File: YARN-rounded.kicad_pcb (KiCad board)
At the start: 2 copper layers, 99 x 91.7 mm, 12 parts, among them J1 Cart System Out, J2 Cart Main In, J3 Cart Sub In, SW1 SW_SPDT, U1 74HC244, U2 74HC244

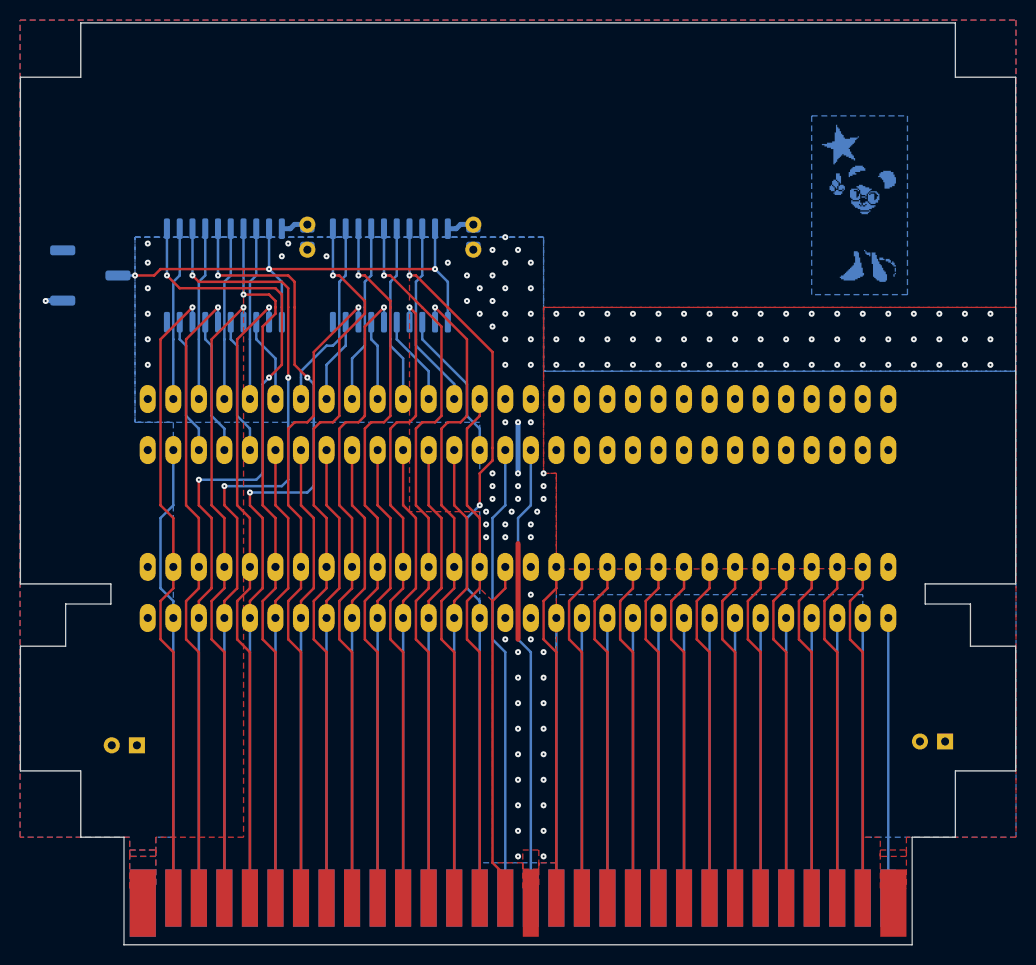
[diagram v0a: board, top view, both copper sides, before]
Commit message: Use bus buffers instead of decoding logic
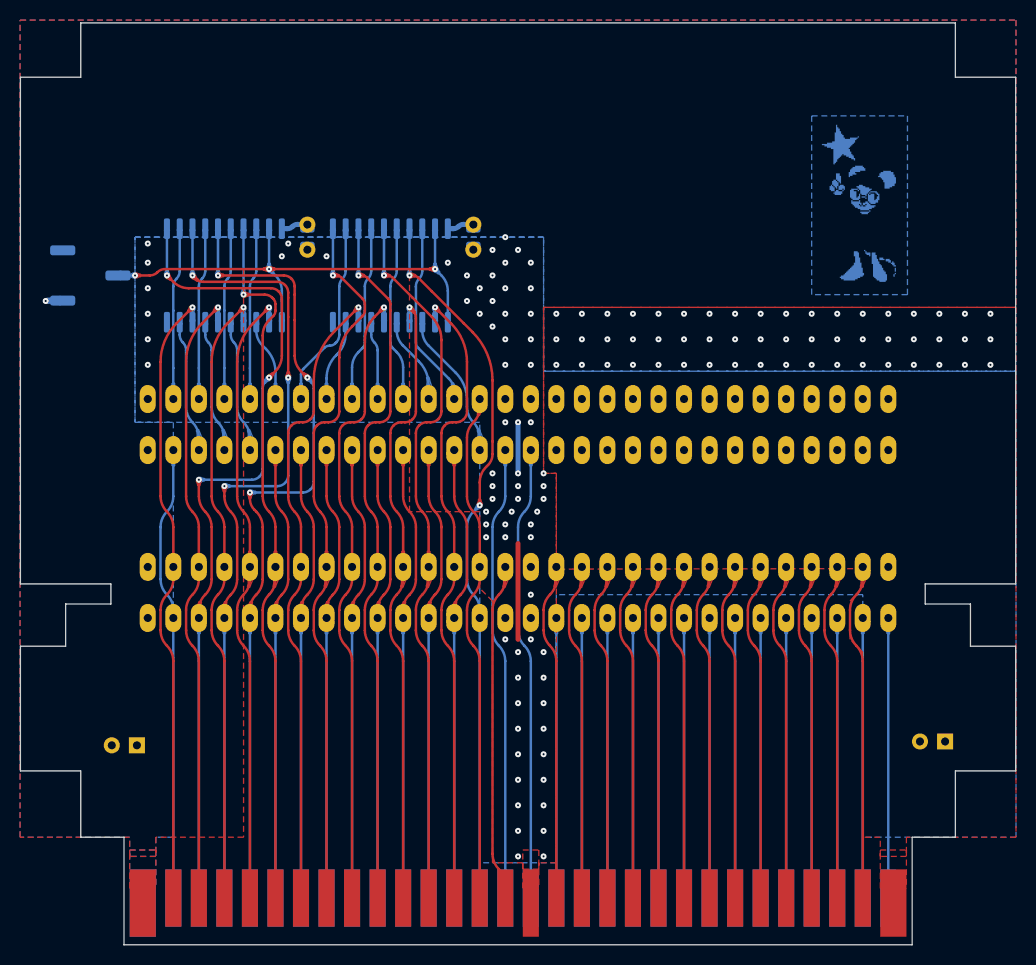
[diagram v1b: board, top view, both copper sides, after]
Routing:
- net /CPU_A6: track 65.4 -> 64.3 mm
- net /CPU_A5: track 72.7 -> 71.5 mm
- net /CPU_A0: track 64.9 -> 63.8 mm
- net /CPU_A1: track 72.7 -> 71.7 mm
- net /CPU_A4: track 64.4 -> 63.4 mm
- net /CPU_A3: track 71.6 -> 70.7 mm
- net /CPU_A2: track 63.9 -> 63.0 mm
- net /CPU_A9: track 63.1 -> 62.2 mm
- net /CPU_A11: track 63.1 -> 62.2 mm
- net /CPU_A10: track 63.1 -> 62.2 mm
- net /CPU_A8: track 63.1 -> 62.2 mm
- net /CPU_A12: track 84.7 -> 83.8 mm
- net /CPU_A7: track 71.5 -> 70.6 mm
- net /~{ROMSEL}: track 71.9 -> 71.1 mm
- net /CPU_R~{W}: track 51.7 -> 50.9 mm
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
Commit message: Buffer data and addr bus, add switch for VRC6 A/B
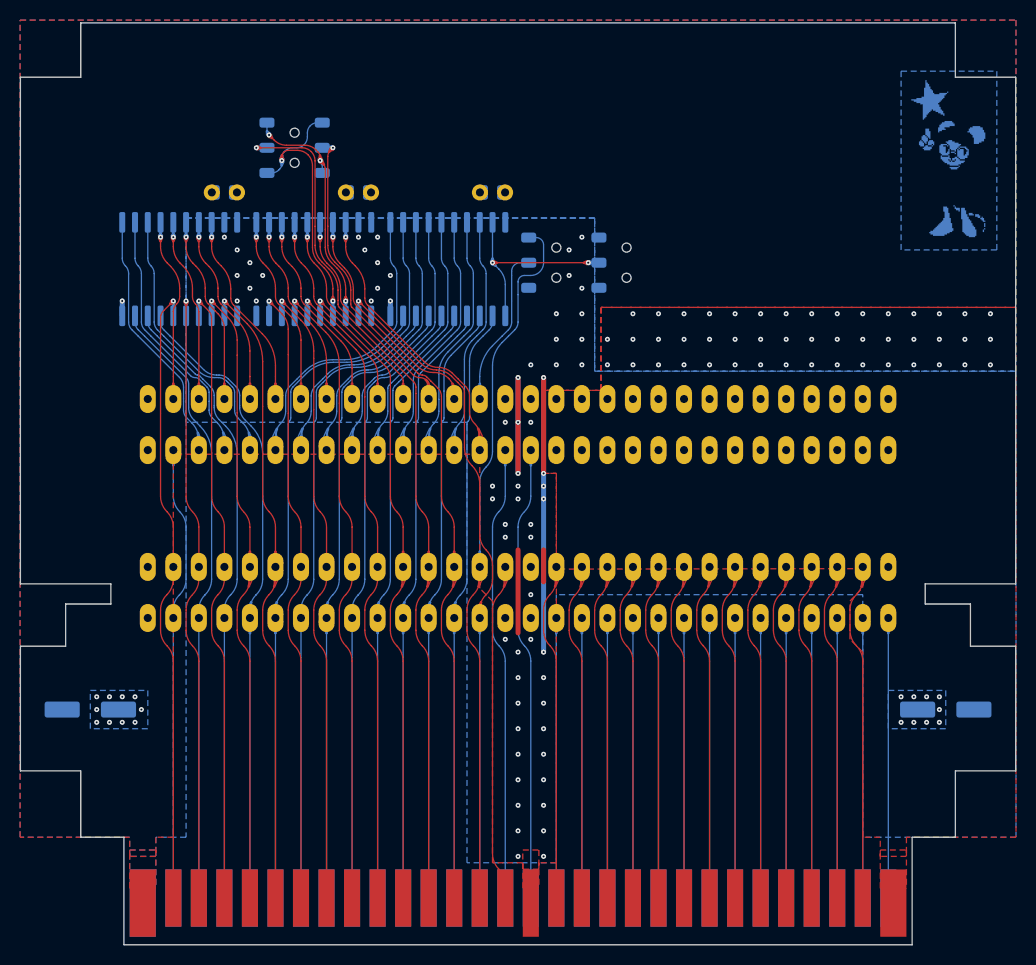
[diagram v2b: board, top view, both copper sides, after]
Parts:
- removed the C4 at (106.0, 67.3)
- added C2: 0.1uF, YARN:C_Disc-0805_D3.0mm_W1.6mm_P2.50mm, B.Cu at (111.1, 62.9)
- added C3: 0.1uF, YARN:C_Disc-0805_D3.0mm_W1.6mm_P2.50mm, B.Cu at (97.8, 62.9)
- added SW2: SW_SPDT, YARN:SK-3390A-L0, B.Cu at (130.8, 69.8)
- added SW3: SW_DPDT_x2, YARN:SS-3390S-L0, B.Cu at (104.8, 58.4)
- added U3: 74HC541, Package_SO:SOIC-20W_7.5x12.8mm_P1.27mm, B.Cu at (93.3, 70.5)
- C4: renamed from C2; footprint Capacitor_THT:CP_Radial_D5.0mm_P2.50mm -> Capacitor_SMD:CP_Elec_6.3x5.4
- C5: renamed from C3; footprint Capacitor_THT:CP_Radial_D5.0mm_P2.50mm -> Capacitor_SMD:CP_Elec_6.3x5.4
- J3: value Cart Sub In -> Cart Exp In
- LOGO-2: renamed from Ref**; value Val** -> YARN
- SW1: footprint YARN:JS102011SCQN -> YARN:SK-3390A-L0
- U1, U2: value 74HC244 -> 74HC541
- moved SW1 53.4 mm to (137.8, 69.8), turned to -90 degrees
- moved LOGO-2 11.4 mm to (149.9, 57.8)
- moved LOGO-1 9.94 mm to (169.5, 59.7)
- moved U2 8.91 mm to (106.7, 70.5)
- moved C5 5.84 mm to (84.5, 114.3), turned to 0 degrees
- moved U1 5.75 mm to (120.0, 70.5)
- moved C1 4.84 mm to (124.5, 62.9), turned to 180 degrees
- moved C4 3.18 mm to (169.5, 114.3), turned to 0 degrees
- renumbered REF** to LOGO-1
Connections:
- J3 pad 14: /CPU_R~{W} -> /S_CPU_R~{W}
- J3 pad 36: /CPU_D7 -> /S_CPU_D7
- J3 pad 37: /CPU_D6 -> /S_CPU_D6
- J3 pad 38: /CPU_D5 -> /S_CPU_D5
- J3 pad 39: /CPU_D4 -> /S_CPU_D4
- J3 pad 40: /CPU_D3 -> /S_CPU_D3
- J3 pad 41: /CPU_D2 -> /S_CPU_D2
- J3 pad 42: /CPU_D1 -> /S_CPU_D1
- J3 pad 43: /CPU_D0 -> /S_CPU_D0
- U1 pad 11: /CPU_A5 -> /S_CPU_D7
- U1 pad 12: /S_CPU_A6 -> /S_CPU_D6
- U1 pad 13: /CPU_A3 -> /S_CPU_D5
- U1 pad 14: /S_CPU_A4 -> /S_CPU_D4
- U1 pad 15: /CPU_A1 -> /S_CPU_D3
- U1 pad 16: /S_CPU_A2 -> /S_CPU_D2
- U1 pad 17: /~{ROMSEL} -> /S_CPU_D1
- U1 pad 18: /S_CPU_A0 -> /S_CPU_D0
- U1 pad 2: /CPU_A0 -> /CPU_D0
- U1 pad 3: /S_~{ROMSEL} -> /CPU_D1
- U1 pad 4: /CPU_A2 -> /CPU_D2
- U1 pad 5: /S_CPU_A1 -> /CPU_D3
- U1 pad 6: /CPU_A4 -> /CPU_D4
- U1 pad 7: /S_CPU_A3 -> /CPU_D5
- U1 pad 8: /CPU_A6 -> /CPU_D6
- U1 pad 9: /S_CPU_A5 -> /CPU_D7
- U2 pad 1: /S_~{CE} -> GND
- U2 pad 11: /CPU_A12 -> /S_CPU_A6
- U2 pad 12: /S_CPU_A11 -> /S_CPU_A5
- U2 pad 13: /CPU_A13 -> /S_CPU_A4
- U2 pad 14: /S_CPU_A10 -> /S_CPU_A3
- U2 pad 15: /CPU_A14 -> /S_CPU_A2
- U2 pad 16: /S_CPU_A9 -> /S_CPU_A1
- U2 pad 17: /CPU_A7 -> /S_CPU_A0
- U2 pad 18: /S_CPU_A8 -> /S_~{ROMSEL}
- U2 pad 19: /S_~{CE} -> GND
- U2 pad 2: /CPU_A8 -> /~{ROMSEL}
- U2 pad 3: /S_CPU_A7 -> /CPU_A0_V
- U2 pad 4: /CPU_A9 -> /CPU_A1_V
- U2 pad 5: /S_CPU_A14 -> /CPU_A2
- U2 pad 6: /CPU_A10 -> /CPU_A3
- U2 pad 7: /S_CPU_A13 -> /CPU_A4
- U2 pad 8: /CPU_A11 -> /CPU_A5
- U2 pad 9: /S_CPU_A12 -> /CPU_A6
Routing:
- net GND: track 16.3 -> 70.3 mm, vias 73 -> 76
- net /S_~{CE}: track 51.1 -> 20.3 mm, vias 3 -> 2
- net /S_CPU_D7: track 0.00 -> 29.9 mm
- net /CPU_A1_V: track 0.00 -> 28.9 mm, vias 0 -> 2
- net /S_CPU_D6: track 0.00 -> 28.7 mm
- net /S_CPU_D5: track 0.00 -> 27.5 mm
- net /S_CPU_D4: track 0.00 -> 26.4 mm
- net /S_CPU_D3: track 0.00 -> 25.5 mm
- net /CPU_A0_V: track 0.00 -> 25.1 mm, vias 0 -> 3
- net /S_CPU_D2: track 0.00 -> 24.9 mm
- net /S_CPU_D1: track 0.00 -> 24.3 mm
- net /S_CPU_D0: track 0.00 -> 23.8 mm
- net /CPU_A12: track 83.8 -> 61.0 mm, vias 3 -> 0
- net /CPU_D7: track 45.2 -> 65.3 mm
- net /CPU_A13: track 81.7 -> 61.7 mm, vias 3 -> 0
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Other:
- board text added: "Dx PASS Dx Z"
- board text added: "R~{W} PASS ~{W}"
- board text added: "VRC6B VRC6A"

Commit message: Improve slide switch footprints
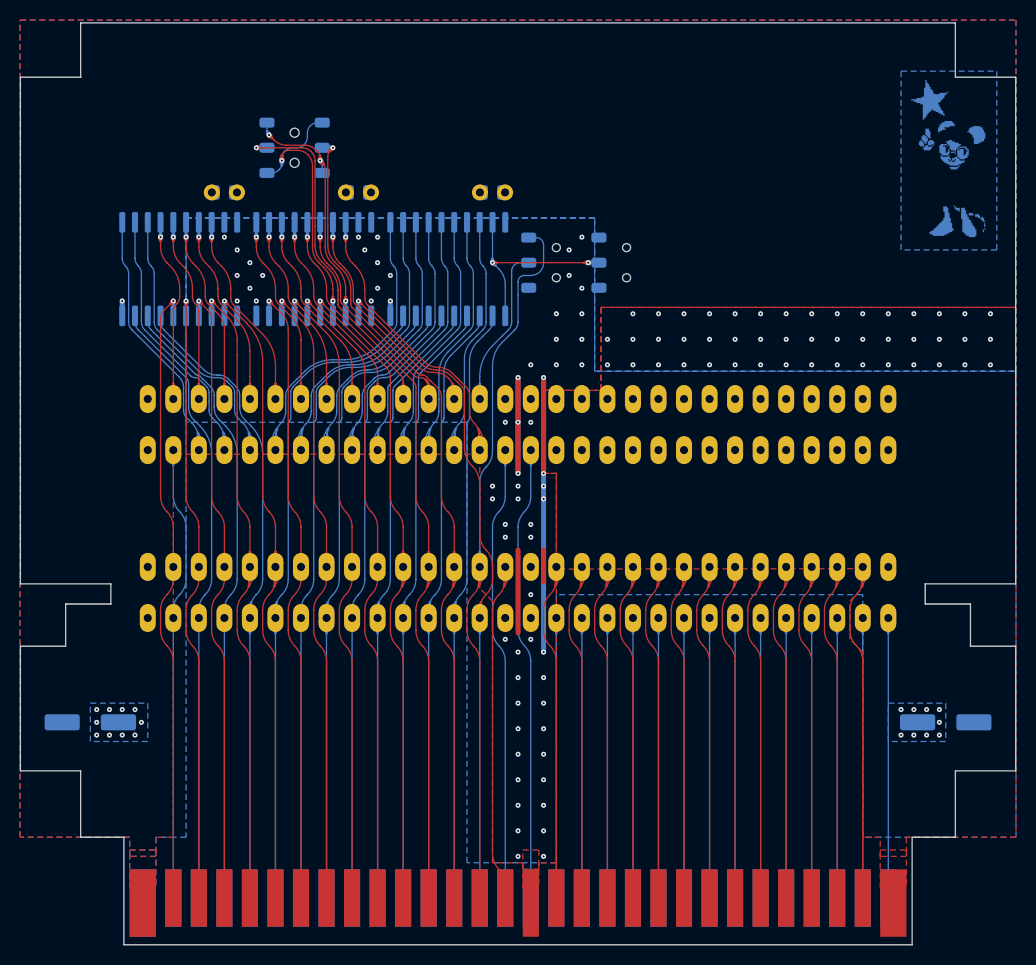
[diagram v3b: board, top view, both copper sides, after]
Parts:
- moved C4 1.27 mm to (169.5, 115.6)
- moved C5 1.27 mm to (84.5, 115.6)

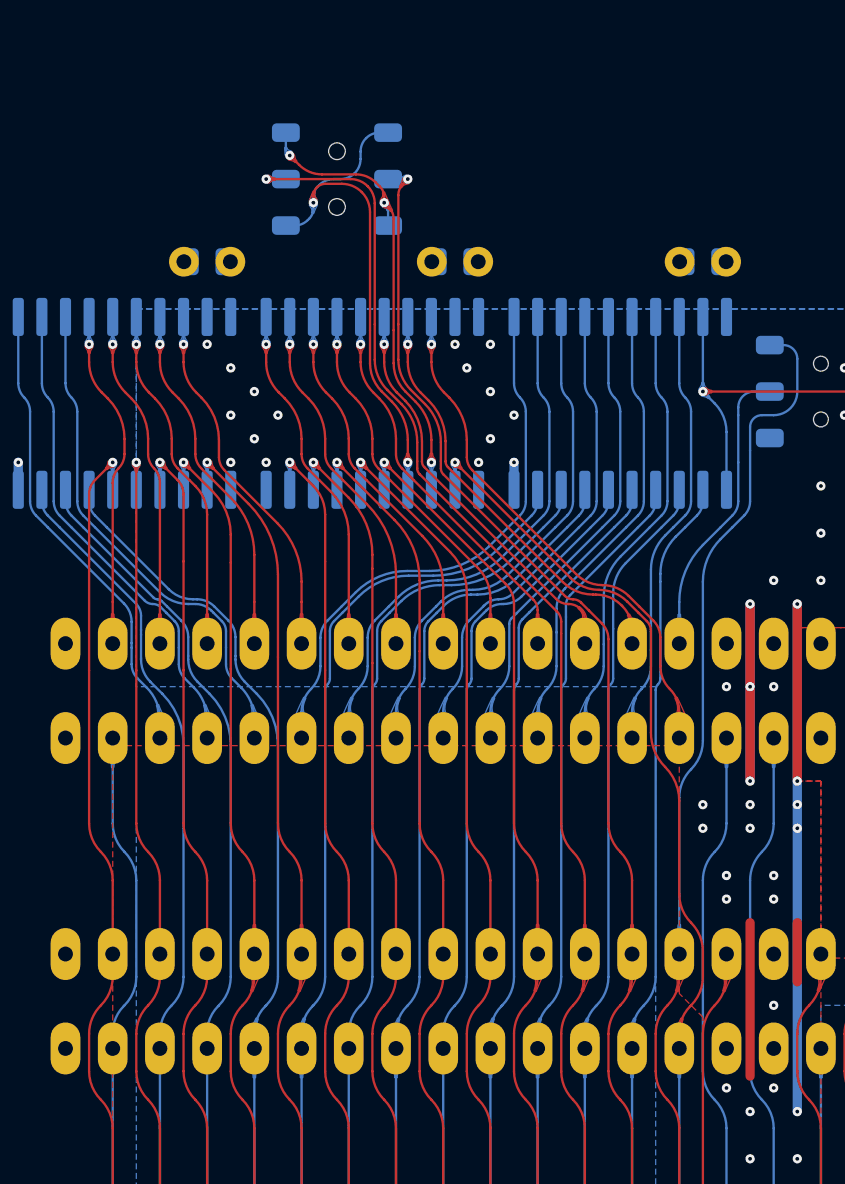
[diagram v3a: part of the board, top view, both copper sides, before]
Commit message: SS-3390S-L0 has slightly different dimensions
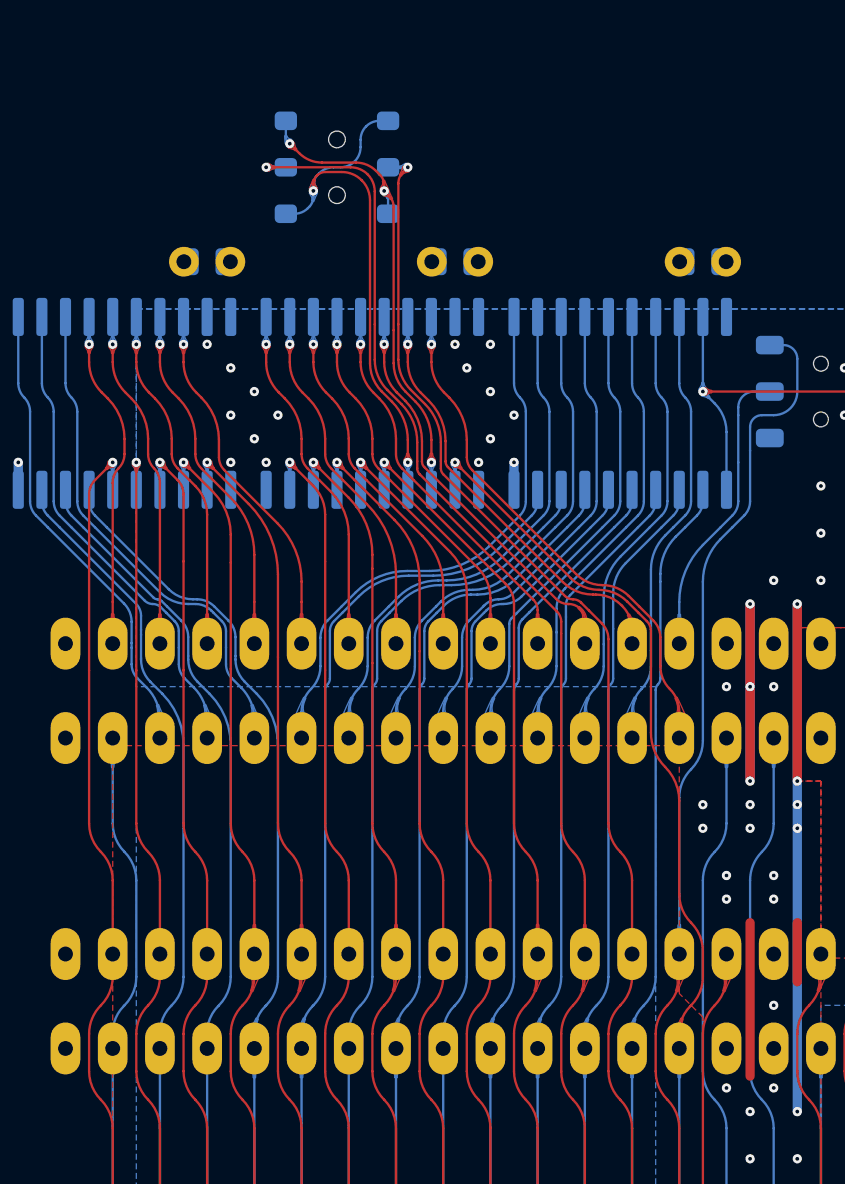
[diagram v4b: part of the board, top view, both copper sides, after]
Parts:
- moved SW3 0.64 mm to (104.8, 57.8)
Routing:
- net /CPU_A0: track 81.4 -> 82.0 mm
- net /CPU_A1: track 85.8 -> 86.4 mm
- net /CPU_A1_V: track 28.9 -> 29.5 mm
- net /CPU_A0_V: track 25.1 -> 25.8 mm
